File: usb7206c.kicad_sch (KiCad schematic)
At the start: 89 parts, among them CN6 W25Q128FVIQ_Connector, U16 USB7206C-I_KDX, U19 25MHz, U20 UCS2113-1-V_G4, U21 MIC23201YML-TR, U22 1uH

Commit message: Preliminary design of USB2244i USB2.0 -> SD converter
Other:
- company: (none) -> Designed by: Matthew Kong
- title: (none) -> USB7206C - USB 3.2g2 Hub Circuit
- moved on the sheet: C136, C137, C138, C139, C140, C141, C142, C143, C144, C145, C146, C147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

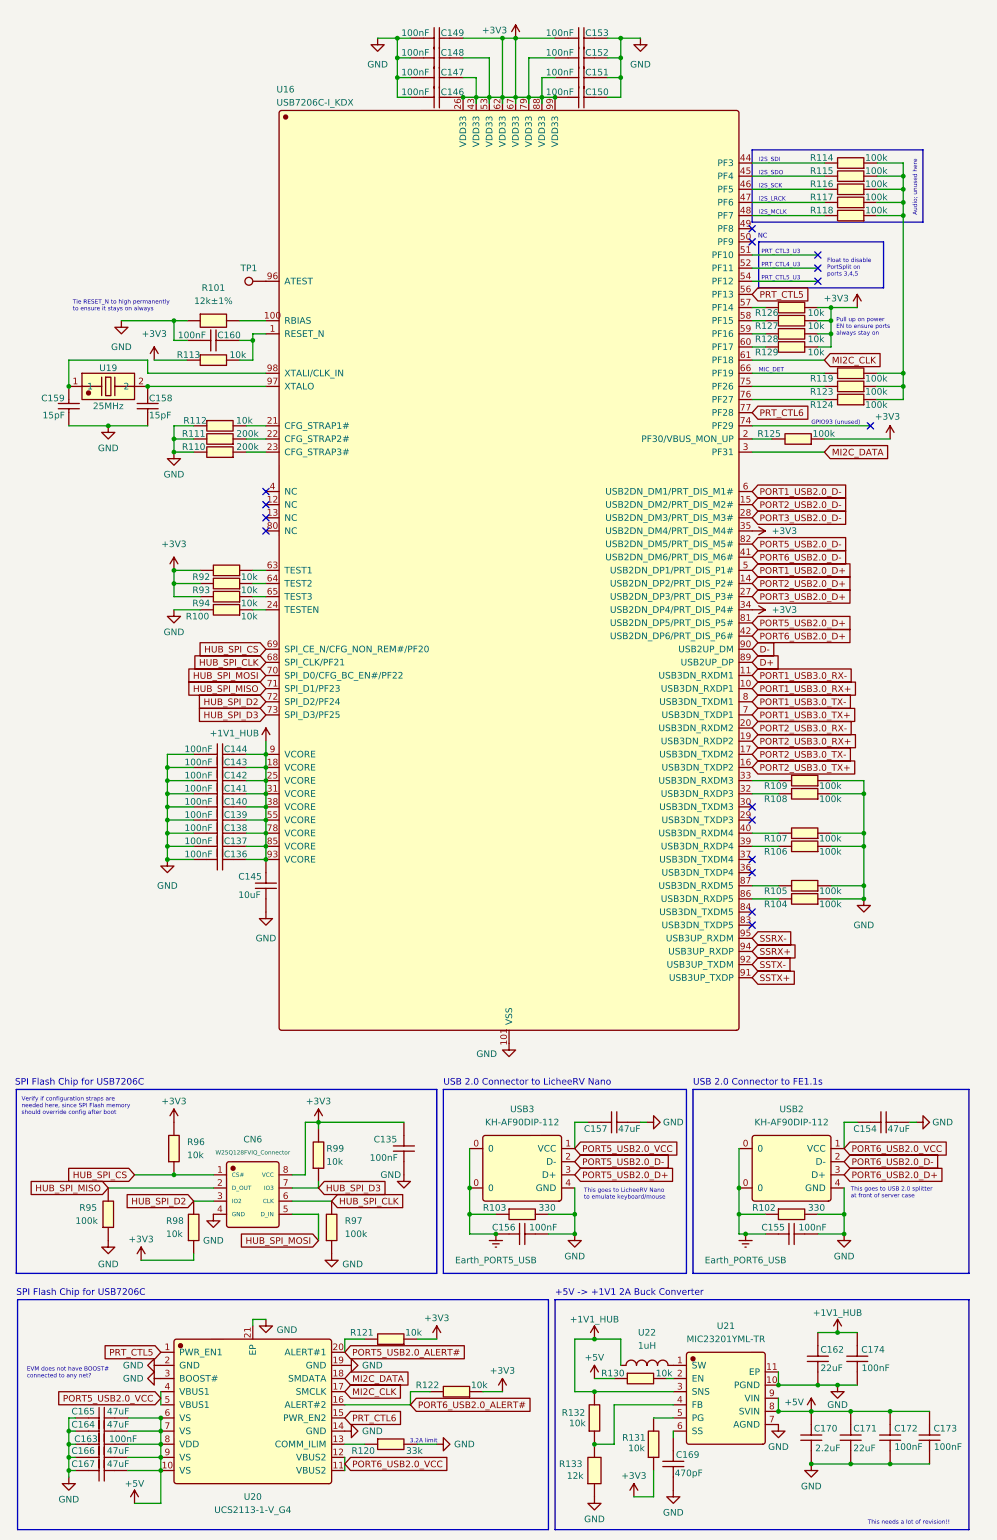
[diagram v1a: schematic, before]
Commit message: Mostly complete initial transfer to hierarchical schematic
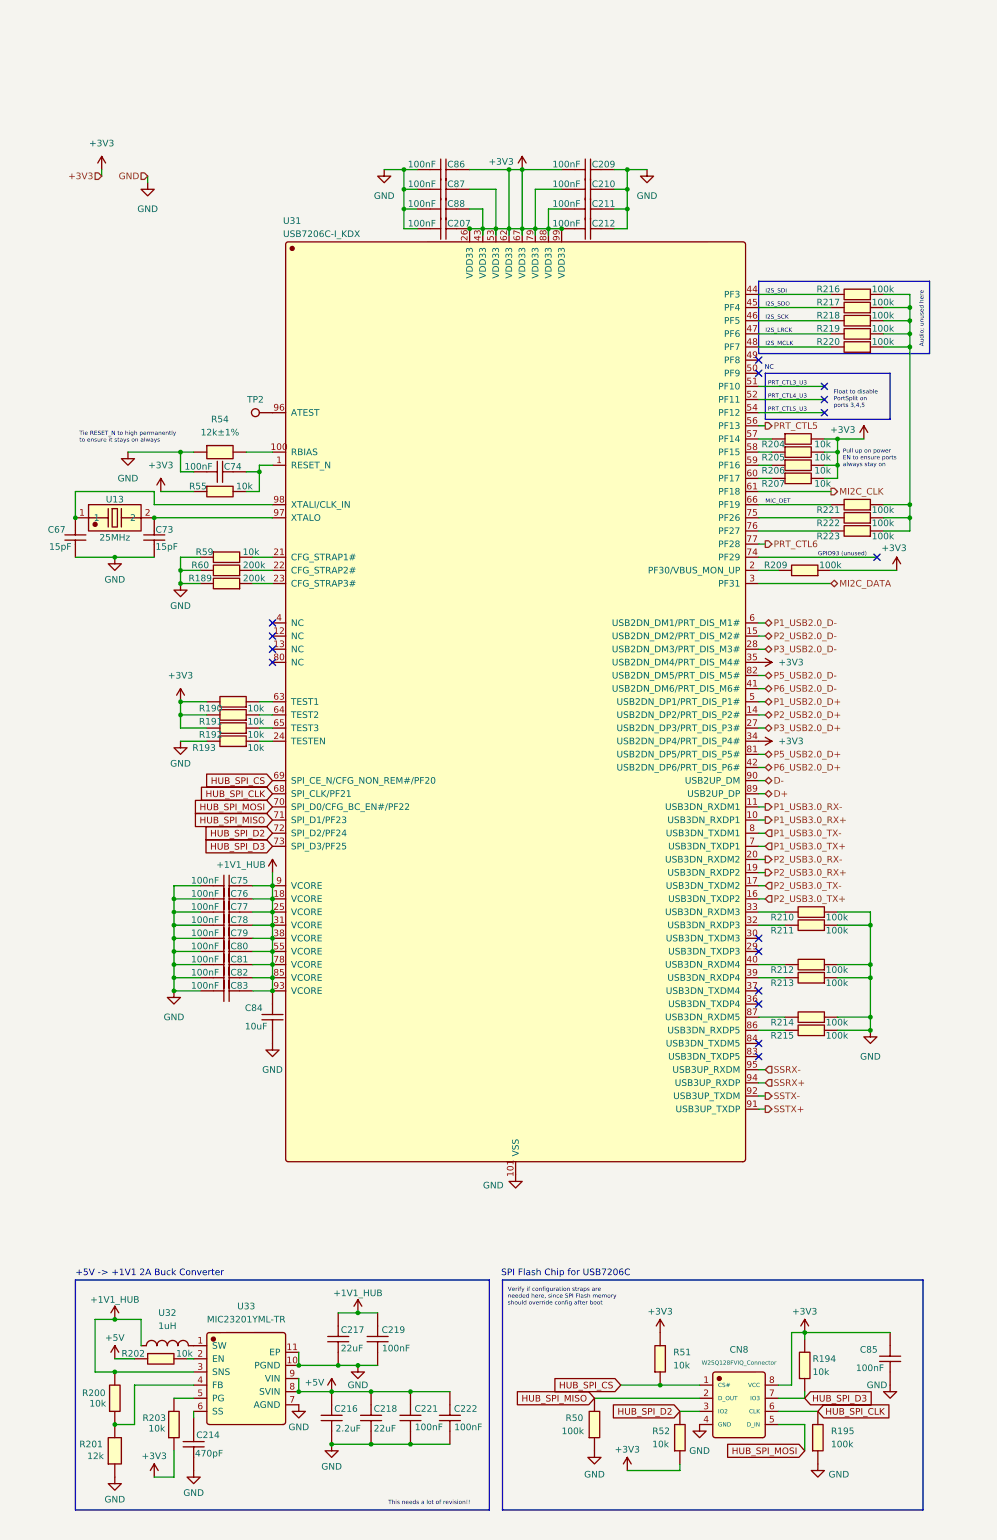
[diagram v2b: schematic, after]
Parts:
- removed C135, C136, C137, C138, C139, C140, C141, C142, C143, C144, C146, C147, C148, C149, C150, C151, C152, C153, C155, C156, C160, C163, C172, C173, C174: 100nF, Capacitor_SMD:C_0402_1005Metric, symbol JLCImport:CL05B104KB54PNC
- removed C145: 10uF, Capacitor_SMD:C_0805_2012Metric, symbol JLCImport:CL21A106KAYNNNE
- removed C154, C157, C164, C165, C166, C167: 47uF, Capacitor_SMD:C_1206_3216Metric, symbol JLCImport:CL31A476MPHNNNE
- removed C158, C159: 15pF, Capacitor_SMD:C_0402_1005Metric, symbol JLCImport:0402CG150J500NT
- removed C162, C171: 22uF, Capacitor_SMD:C_0603_1608Metric, symbol JLCImport:CL10A226MQ8NRNC
- removed C169: 470pF, Capacitor_SMD:C_0402_1005Metric, symbol JLCImport:TCC0402X7R471K500AT
- removed C170: 2.2uF, Capacitor_SMD:C_0402_1005Metric, symbol JLCImport:JMK105BJ225MVHF
- removed CN6: W25Q128FVIQ_Connector, JLCImport:H2541FV-C762-2X04P, symbol JLCImport:H2541FV-C762-2X04P
- removed R100, R112, R113, R121, R122, R126, R127, R128, R129, R130, R131, R132, R92, R93, R94, R96, R98, R99: 10k, Resistor_SMD:R_0402_1005Metric, symbol JLCImport:0402WGF1002TCE
- removed R101: 12k±1%, Resistor_SMD:R_0402_1005Metric, symbol JLCImport:CR0402F12K0Q10Z
- removed R102, R103: 330, Resistor_SMD:R_0402_1005Metric, symbol JLCImport:0402WGF3300TCE
- removed R104, R105, R106, R107, R108, R109, R114, R115, R116, R117, R118, R119, R123, R124, R125, R95, R97: 100k, Resistor_SMD:R_0402_1005Metric, symbol JLCImport:0402WGF1003TCE
- removed R110, R111: 200k, Resistor_SMD:R_0603_1608Metric, symbol JLCImport:0603WAF2003T5E
- removed R120: 33k, Resistor_SMD:R_0402_1005Metric, symbol JLCImport:WR04X3302FTL
- removed R133: 12k, Resistor_SMD:R_0402_1005Metric, symbol JLCImport:CR0402F12K0Q10Z
- removed TP1: A, TestPoint:TestPoint_Pad_1.0x1.0mm, symbol Connector:TestPoint
- removed U16: USB7206C-I_KDX, JLCImport:USB7206C-I_KDX, symbol JLCImport:USB7206C-I_KDX
- removed U19: 25MHz, JLCImport:25M_10PF_50PPM, symbol JLCImport:25M_10PF_50PPM
- removed U20: UCS2113-1-V_G4, JLCImport:UCS2113-1-V_G4, symbol JLCImport:UCS2113-1-V_G4
- removed U21: MIC23201YML-TR, JLCImport:MIC23201YML-TR, symbol JLCImport:MIC23201YML-TR
- removed U22: 1uH, TerminalBlock_Phoenix:TerminalBlock_Phoenix_PTSM-0,5-2-2,5-V-SMD_1x02-1MP_P2.50mm_Vertical, symbol JLCImport:FTC252012S1R0MBCA
- removed USB2, USB3: KH-AF90DIP-112, JLCImport:KH-AF90DIP-112, symbol JLCImport:KH-AF90DIP-112
- added C207, C209, C210, C211, C212, C219, C221, C222, C74, C75, C76, C77, C78, C79, C80, C81, C82, C83, C85, C86, C87, C88: 100nF, Capacitor_SMD:C_0402_1005Metric, symbol JLCImport:CL05B104KB54PNC
- added C214: 470pF, Capacitor_SMD:C_0402_1005Metric, symbol JLCImport:TCC0402X7R471K500AT
- added C216: 2.2uF, Capacitor_SMD:C_0402_1005Metric, symbol JLCImport:JMK105BJ225MVHF
- added C217, C218: 22uF, Capacitor_SMD:C_0603_1608Metric, symbol JLCImport:CL10A226MQ8NRNC
- added C67, C73: 15pF, Capacitor_SMD:C_0402_1005Metric, symbol JLCImport:0402CG150J500NT
- added C84: 10uF, Capacitor_SMD:C_0805_2012Metric, symbol JLCImport:CL21A106KAYNNNE
- added CN8: W25Q128FVIQ_Connector, JLCImport:H2541FV-C762-2X04P, symbol JLCImport:H2541FV-C762-2X04P
- added R189, R60: 200k, Resistor_SMD:R_0603_1608Metric, symbol JLCImport:0603WAF2003T5E
- added R190, R191, R192, R193, R194, R200, R202, R203, R204, R205, R206, R207, R51, R52, R55, R59: 10k, Resistor_SMD:R_0402_1005Metric, symbol JLCImport:0402WGF1002TCE
- added R195, R209, R210, R211, R212, R213, R214, R215, R216, R217, R218, R219, R220, R221, R222, R223, R50: 100k, Resistor_SMD:R_0402_1005Metric, symbol JLCImport:0402WGF1003TCE
- added R201: 12k, Resistor_SMD:R_0402_1005Metric, symbol JLCImport:CR0402F12K0Q10Z
- added R54: 12k±1%, Resistor_SMD:R_0402_1005Metric, symbol JLCImport:CR0402F12K0Q10Z
- added TP2: A, TestPoint:TestPoint_Pad_1.0x1.0mm, symbol Connector:TestPoint
- added U13: 25MHz, JLCImport:25M_10PF_50PPM, symbol JLCImport:25M_10PF_50PPM
- added U31: USB7206C-I_KDX, JLCImport:USB7206C-I_KDX, symbol JLCImport:USB7206C-I_KDX
- added U32: 1uH, TerminalBlock_Phoenix:TerminalBlock_Phoenix_PTSM-0,5-2-2,5-V-SMD_1x02-1MP_P2.50mm_Vertical, symbol JLCImport:FTC252012S1R0MBCA
- added U33: MIC23201YML-TR, JLCImport:MIC23201YML-TR, symbol JLCImport:MIC23201YML-TR
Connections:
- net +1V1_HUB: now also C217.2, C219.2, C75.1, C76.1, C77.1, C78.1, C79.1, C80.1, C81.1, C82.1, C83.1, C84.2, R200.2, U31.18 (VCORE), U31.25 (VCORE), U31.31 (VCORE), U31.38 (VCORE), U31.55 (VCORE), U31.78 (VCORE), U31.85 (VCORE), U31.9 (VCORE), U31.93 (VCORE), U32.1, U33.3 (SNS)
- net +3V3: now also C207.1, C209.2, C210.2, C211.2, C212.2, C85.2, C86.1, C87.1, C88.1, CN8.8 (VCC), R190.2, R191.2, R192.2, R194.2, R203.1, R204.2, R205.2, R206.2, R207.2, R209.1, R51.2, R52.1, R55.1, U31.26 (VDD33), U31.34 (USB2DN_DP4/PRT_DIS_P4#), U31.35 (USB2DN_DM4/PRT_DIS_M4#), U31.43 (VDD33), U31.53 (VDD33), U31.62 (VDD33), U31.67 (VDD33), U31.79 (VDD33), U31.88 (VDD33), U31.99 (VDD33)
- net +5V: now also C216.2, C218.2, C221.2, C222.2, R202.1, U33.8 (SVIN), U33.9 (VIN)
- net D+: now also U31.89 (USB2UP_DP)
- net D-: now also U31.90 (USB2UP_DM)
- net GND: now also C207.2, C209.1, C210.1, C211.1, C212.1, C214.1, C216.1, C217.1, C218.1, C219.1, C221.1, C222.1, C67.1, C73.1, C74.2, C75.2, C76.2, C77.2, C78.2, C79.2, C80.2, C81.2, C82.2, C83.2, C84.1, C85.1, C86.2, C87.2, C88.2, CN8.4 (GND), R189.2, R193.2, R195.1, R201.1, R210.1, R211.1, R212.1, R213.1, R214.1, R215.1, R50.1, R54.1, R59.1, R60.2, U31.101 (VSS), U33.10 (PGND), U33.11 (EP), U33.7 (AGND)
- net HUB_SPI_CLK: now also CN8.6 (CLK), R195.2, U31.68 (SPI_CLK/PF21)
- net HUB_SPI_CS: now also CN8.1 (CS#), R51.1, U31.69 (SPI_CE_N/CFG_NON_REM#/PF20)
- net HUB_SPI_D2: now also CN8.3 (IO2), R52.2, U31.72 (SPI_D2/PF24)
- net HUB_SPI_D3: now also CN8.7 (IO3), R194.1, U31.73 (SPI_D3/PF25)
- net HUB_SPI_MISO: now also CN8.2 (D_OUT), R50.2, U31.71 (SPI_D1/PF23)
- net HUB_SPI_MOSI: now also CN8.5 (D_IN), U31.70 (SPI_D0/CFG_BC_EN#/PF22)
- net MI2C_CLK: now also U31.61 (PF18)
- net MI2C_DATA: now also U31.3 (PF31)
- net PRT_CTL5: now also U31.56 (PF13)
- net PRT_CTL6: now also U31.77 (PF28)
- net SSRX+: now also U31.94 (USB3UP_RXDP)
- net SSRX-: now also U31.95 (USB3UP_RXDM)
- net SSTX+: now also U31.91 (USB3UP_TXDP)
- net SSTX-: now also U31.92 (USB3UP_TXDM)
- new net: C74.1, R55.2, U31.1 (RESET_N)
- new net: R216.1, R217.1, R218.1, R219.1, R220.1, R221.1, R222.1, R223.1
- new net: R222.2, U31.75 (PF26)
- new net: R221.2, U31.66 (PF19)
- new net: U32.2, U33.1 (SW)
- new net: C67.2, U13.1, U31.98 (XTALI/CLK_IN)
- new net: C73.2, U13.2, U31.97 (XTALO)
- new net: R220.2, U31.48 (PF7)
- new net: R212.2, U31.40 (USB3DN_RXDM4)
- new net: R54.2, U31.100 (RBIAS)
- new net: R209.2, U31.2 (PF30/VBUS_MON_UP)
- new net: R59.2, U31.21 (CFG_STRAP1#)
- new net: R60.1, U31.22 (CFG_STRAP2#)
- new net: R189.1, U31.23 (CFG_STRAP3#)
- new net: R193.1, U31.24 (TESTEN)
- new net: R211.2, U31.32 (USB3DN_RXDP3)
- new net: R210.2, U31.33 (USB3DN_RXDM3)
- new net: R213.2, U31.39 (USB3DN_RXDP4)
- new net: R216.2, U31.44 (PF3)
- new net: R217.2, U31.45 (PF4)
- new net: R218.2, U31.46 (PF5)
- new net: R219.2, U31.47 (PF6)
- new net: R204.1, U31.57 (PF14)
- new net: R205.1, U31.58 (PF15)
- new net: R206.1, U31.59 (PF16)
- new net: R207.1, U31.60 (PF17)
- new net: R190.1, U31.63 (TEST1)
- new net: R191.1, U31.64 (TEST2)
- new net: R192.1, U31.65 (TEST3)
- new net: R223.2, U31.76 (PF27)
- new net: R215.2, U31.86 (USB3DN_RXDP5)
- new net: R214.2, U31.87 (USB3DN_RXDM5)
- new net: TP2.1, U31.96 (ATEST)
- new net: R202.2, U33.2 (EN)
- new net: R200.1, R201.2, U33.4 (FB)
- new net: R203.2, U33.5 (PG)
- new net: C214.2, U33.6 (SS)
- new net P1_USB2.0_D+: U31.5 (USB2DN_DP1/PRT_DIS_P1#)
- new net P1_USB2.0_D-: U31.6 (USB2DN_DM1/PRT_DIS_M1#)
- new net P1_USB3.0_RX+: U31.10 (USB3DN_RXDP1)
- new net P1_USB3.0_RX-: U31.11 (USB3DN_RXDM1)
- new net P1_USB3.0_TX+: U31.7 (USB3DN_TXDP1)
- new net P1_USB3.0_TX-: U31.8 (USB3DN_TXDM1)
- new net P2_USB2.0_D+: U31.14 (USB2DN_DP2/PRT_DIS_P2#)
- new net P2_USB2.0_D-: U31.15 (USB2DN_DM2/PRT_DIS_M2#)
- new net P2_USB3.0_RX+: U31.19 (USB3DN_RXDP2)
- new net P2_USB3.0_RX-: U31.20 (USB3DN_RXDM2)
- new net P2_USB3.0_TX+: U31.16 (USB3DN_TXDP2)
- new net P2_USB3.0_TX-: U31.17 (USB3DN_TXDM2)
- new net P3_USB2.0_D+: U31.27 (USB2DN_DP3/PRT_DIS_P3#)
- new net P3_USB2.0_D-: U31.28 (USB2DN_DM3/PRT_DIS_M3#)
- new net P5_USB2.0_D+: U31.81 (USB2DN_DP5/PRT_DIS_P5#)
- new net P5_USB2.0_D-: U31.82 (USB2DN_DM5/PRT_DIS_M5#)
- new net P6_USB2.0_D+: U31.42 (USB2DN_DP6/PRT_DIS_P6#)
- new net P6_USB2.0_D-: U31.41 (USB2DN_DM6/PRT_DIS_M6#)
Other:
- note removed: "3.2A limit"
- note removed: "EVM does not have BOOST# connected to any net?"
- note removed: "This goes to LicheeRV Nano to emulate keyboard/mouse"
- note removed: "This goes to USB 2.0 splitter at front of server case"
- note removed: "USB 2.0 Connector to FE1.1s"
- note removed: "USB 2.0 Connector to LicheeRV Nano"

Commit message: Added TVS clamping diodes to upstream USB-C port and fixed RX/TX orientation routing for entire system
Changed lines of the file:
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@@
 	)
 	(hierarchical_label "P1_USB3.0_RX-"
-		(shape output)
+		(shape input)
 		(at 160.02 166.37 0)
 		(effects
@@
 	)
 	(hierarchical_label "P1_USB3.0_TX+"
-		(shape input)
+		(shape output)
 		(at 160.02 173.99 0)
 		(effects
@@
 	)
 	(hierarchical_label "P1_USB3.0_RX+"
-		(shape output)
+		(shape input)
 		(at 160.02 168.91 0)
 		(effects
@@
 	)
 	(hierarchical_label "P1_USB3.0_TX-"
-		(shape input)
+		(shape output)
 		(at 160.02 171.45 0)
 		(effects

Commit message: Changed USB7206C's buck converter to LX7167
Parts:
- removed C214: 470pF, Capacitor_SMD:C_0402_1005Metric, symbol JLCImport:TCC0402X7R471K500AT
- removed C216: 2.2uF, Capacitor_SMD:C_0402_1005Metric, symbol JLCImport:JMK105BJ225MVHF
- removed C217, C218: 22uF, Capacitor_SMD:C_0603_1608Metric, symbol JLCImport:CL10A226MQ8NRNC
- removed C219, C221, C222: 100nF, Capacitor_SMD:C_0402_1005Metric, symbol JLCImport:CL05B104KB54PNC
- removed R200, R202, R203: 10k, Resistor_SMD:R_0402_1005Metric, symbol JLCImport:0402WGF1002TCE
- removed R201: 12k, Resistor_SMD:R_0402_1005Metric, symbol JLCImport:CR0402F12K0Q10Z
- removed U32: 1uH, TerminalBlock_Phoenix:TerminalBlock_Phoenix_PTSM-0,5-2-2,5-V-SMD_1x02-1MP_P2.50mm_Vertical, symbol JLCImport:FTC252012S1R0MBCA
- removed U33: MIC23201YML-TR, JLCImport:MIC23201YML-TR, symbol JLCImport:MIC23201YML-TR
- added C156: 27pF, Capacitor_SMD:C_0402_1005Metric, symbol JLCImport:TCC0402C0G270J500AT
- added C157, C158, C159, C190, C191: 22uF, Capacitor_SMD:C_0603_1608Metric, symbol JLCImport:0603DS226M4R0NT
- added C192, C193: 100nF, Capacitor_SMD:C_0402_1005Metric, symbol JLCImport:CL05B104KB54PNC
- added C194: 1uF, Capacitor_SMD:C_0402_1005Metric, symbol JLCImport:CL05A105KA5NQNC
- added L1: 1uH, JLCImport:PIM201608S1R0MBCA, symbol JLCImport:PIM201608S1R0MBCA
- added R22: 120k, Resistor_SMD:R_0402_1005Metric, symbol JLCImport:HRC0402F1203DNTO
- added R328: 10.0Ω, Resistor_SMD:R_0402_1005Metric, symbol JLCImport:0402WGF100JTCE
- added R336, R8: 100k, Resistor_SMD:R_0402_1005Metric, symbol JLCImport:HP02WAF1003TCE
- added U19: LX7167ACLD-TR, JLCImport:LX7167ACLD-TR, symbol JLCImport:LX7167ACLD-TR
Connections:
- net +3V3: now also C191.2, C192.1, R328.1, R336.2, U19.8 (PVIN)
- net GND: now also C157.1, C158.1, C159.1, C190.1, C191.1, C192.2, C193.2, C194.2, R22.2, U19.1 (PGND), U19.3 (GND), U19.9 (EP)
- net +1V1_HUB renamed +1V1
- net +1V1: now also C156.1, C157.2, C158.2, C159.2, C190.2, L1.1, R8.2
- new net: R336.1, U19.6 (PG)
- new net: C156.2, R22.1, R8.1, U19.4 (FB)
- new net: L1.2, U19.2 (SW)
- new net: C194.1, R328.2, U19.7 (VCC)
- new net USB7206C_EN: C193.1, U19.5 (EN)
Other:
- note added: "+5V -> +1V1 2.4A Buck Converter"
- note removed: "+5V -> +1V1 2A Buck Converter"
- note removed: "This needs a lot of revision!!"
- moved on the sheet: C67, C73, C85, CN8, R194, R195, R50, R51, R52, U13
